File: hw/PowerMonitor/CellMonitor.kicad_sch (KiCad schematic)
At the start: 23 parts, among them Q1 Q_PMOS_GDS, U1 LM393, U13 74LVC1G32

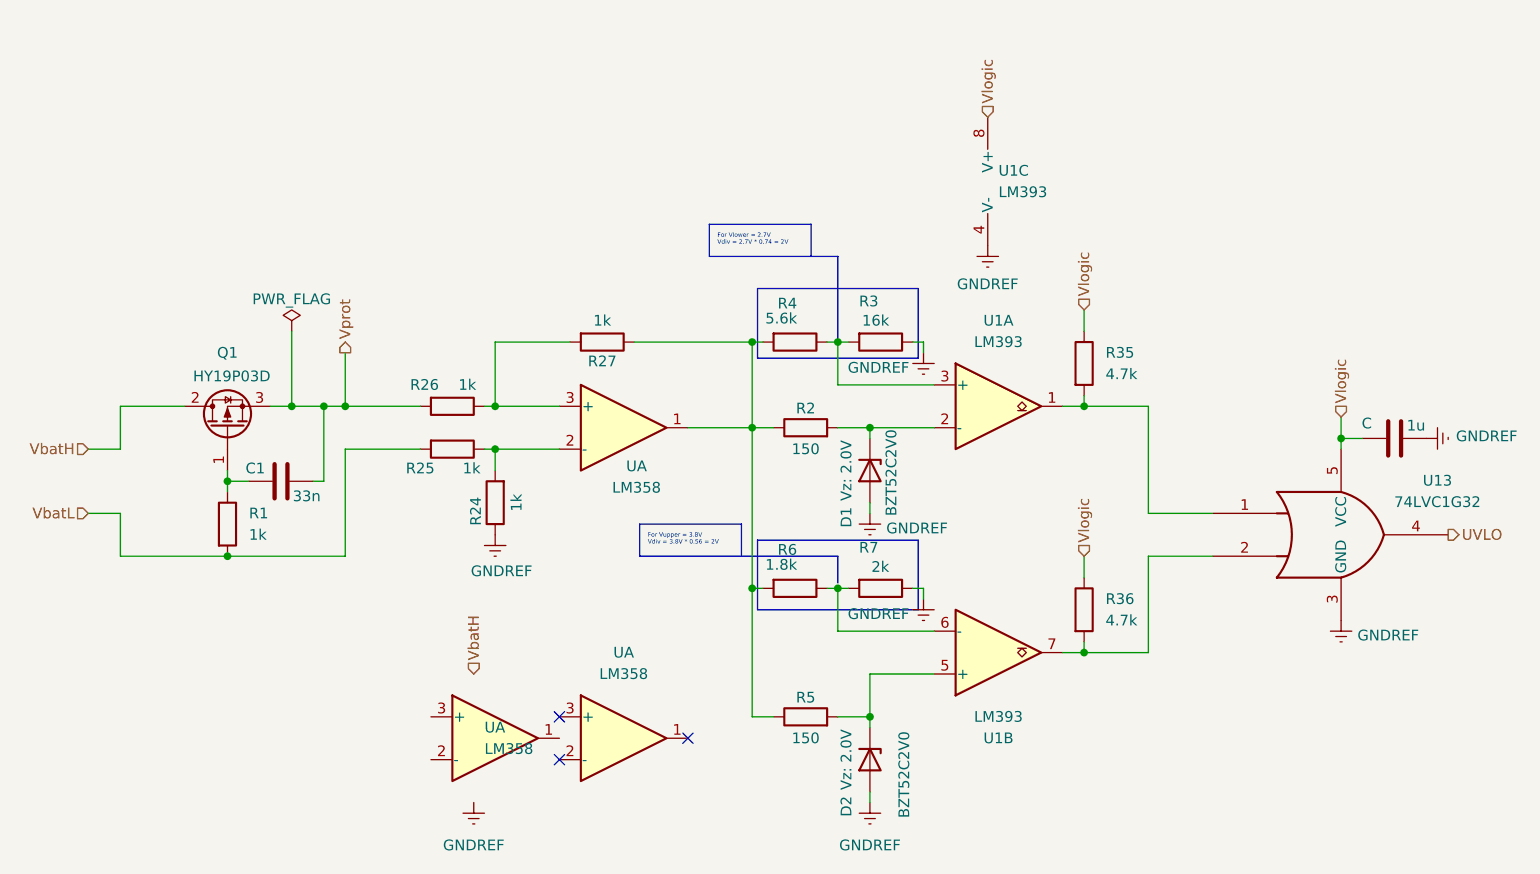
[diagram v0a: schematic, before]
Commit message: preliminar design for battery power monitor, add sd card to fmu
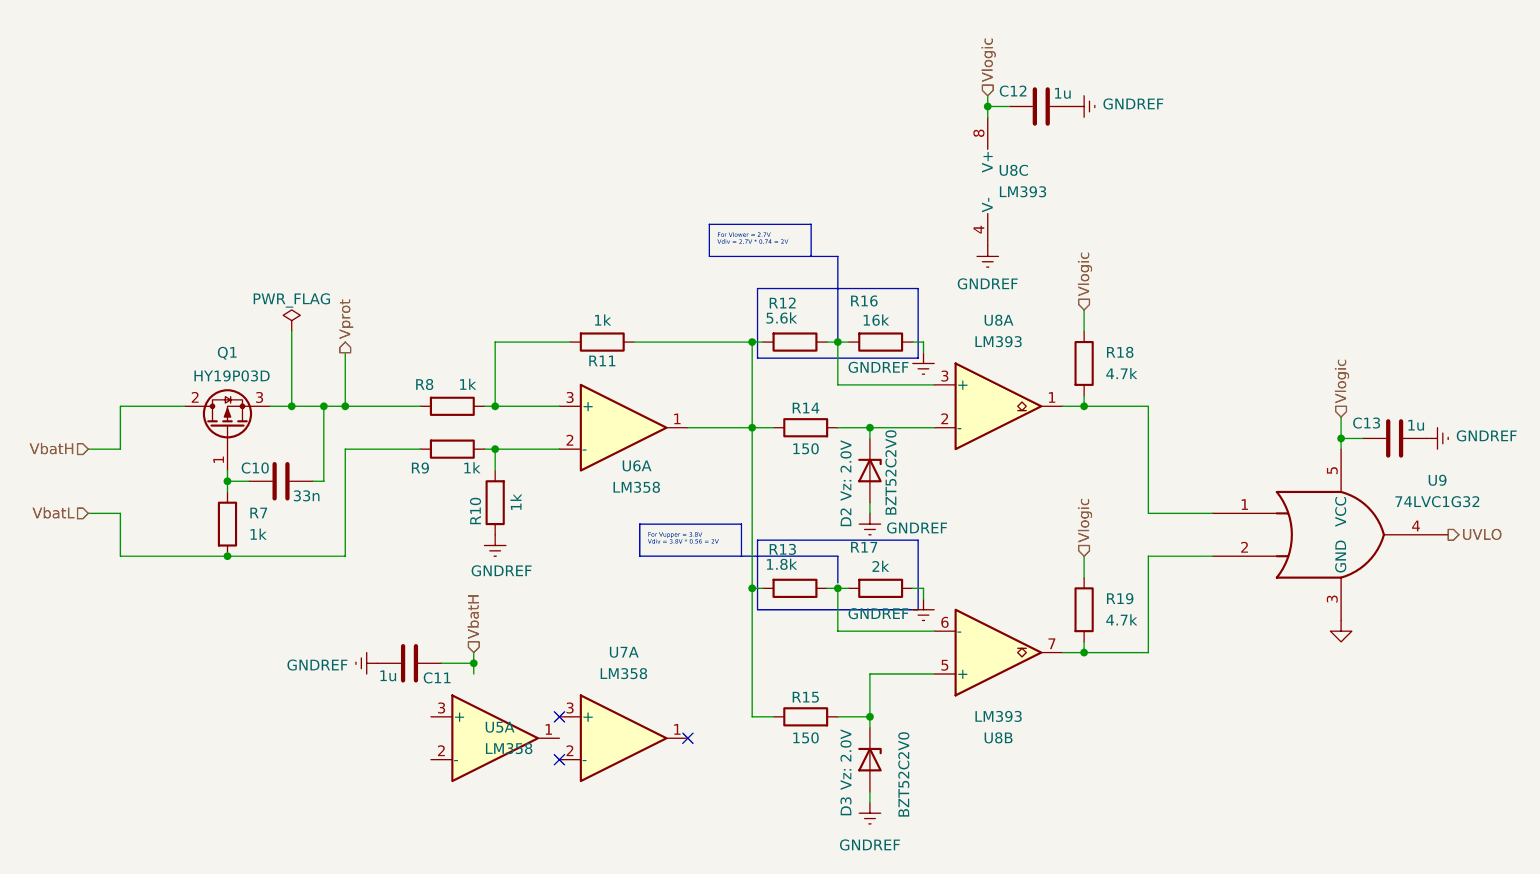
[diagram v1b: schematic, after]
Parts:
- added C11, C12: 1u, Capacitor_SMD:C_0603_1608Metric_Pad1.08x0.95mm_HandSolder, symbol Device:C
- renumbered C1 to C10, C to C13, D1 to D2, D2 to D3, R24 to R10, R27 to R11, R4 to R12, R6 to R13, R2 to R14, R5 to R15, R3 to R16, R7 to R17, R35 to R18, R36 to R19, R1 to R7, R26 to R8, R25 to R9, U to U5, U to U6, U to U7, U1 to U8, U13 to U9
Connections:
- net GNDREF: now also C11.2, C12.2; no longer U9.3 (GND)
- net VbatH: now also C11.1
- net Vlogic: now also C12.1
- new net GND: U9.3 (GND)
